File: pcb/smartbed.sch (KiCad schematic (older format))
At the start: 20 parts, among them U1 ATSAMD21J18A

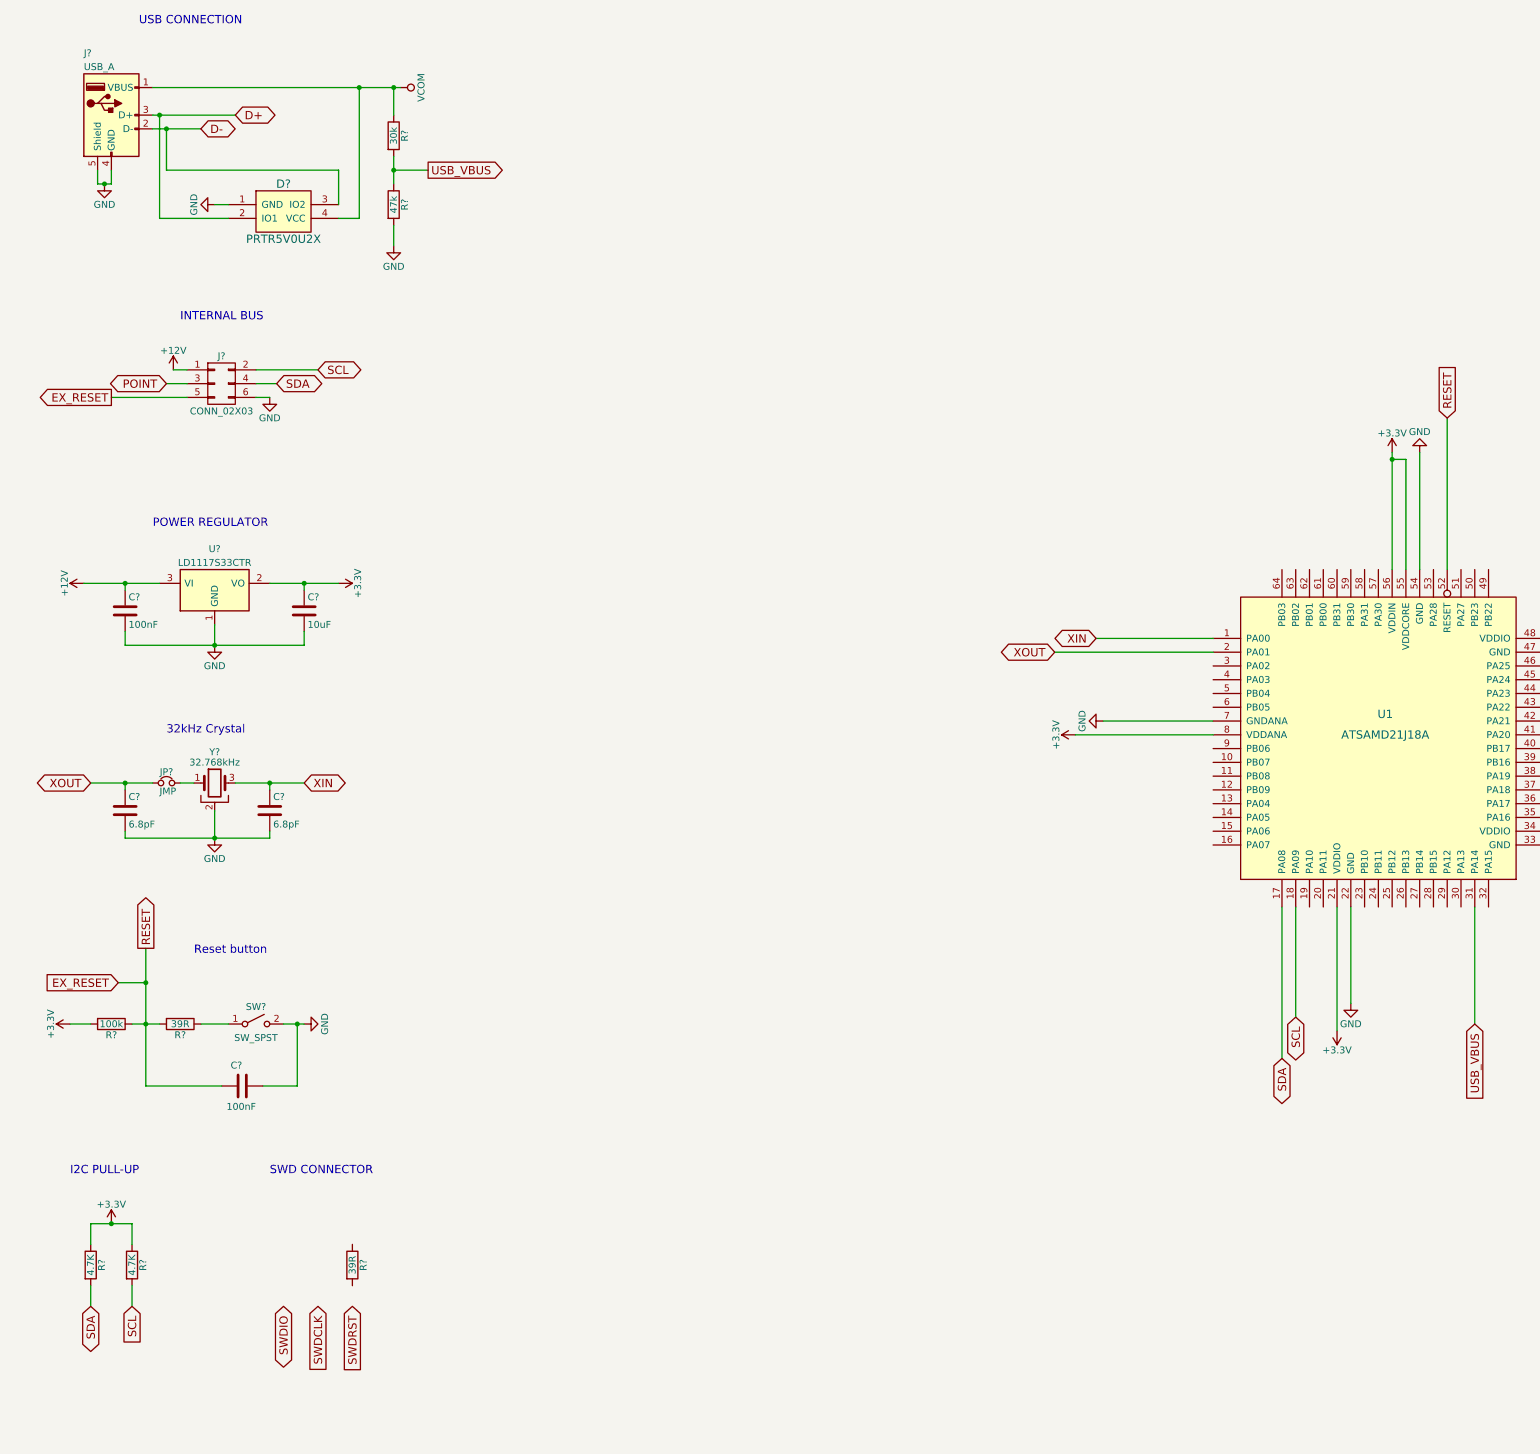
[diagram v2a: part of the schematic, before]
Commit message: Added debug connector and capacitors
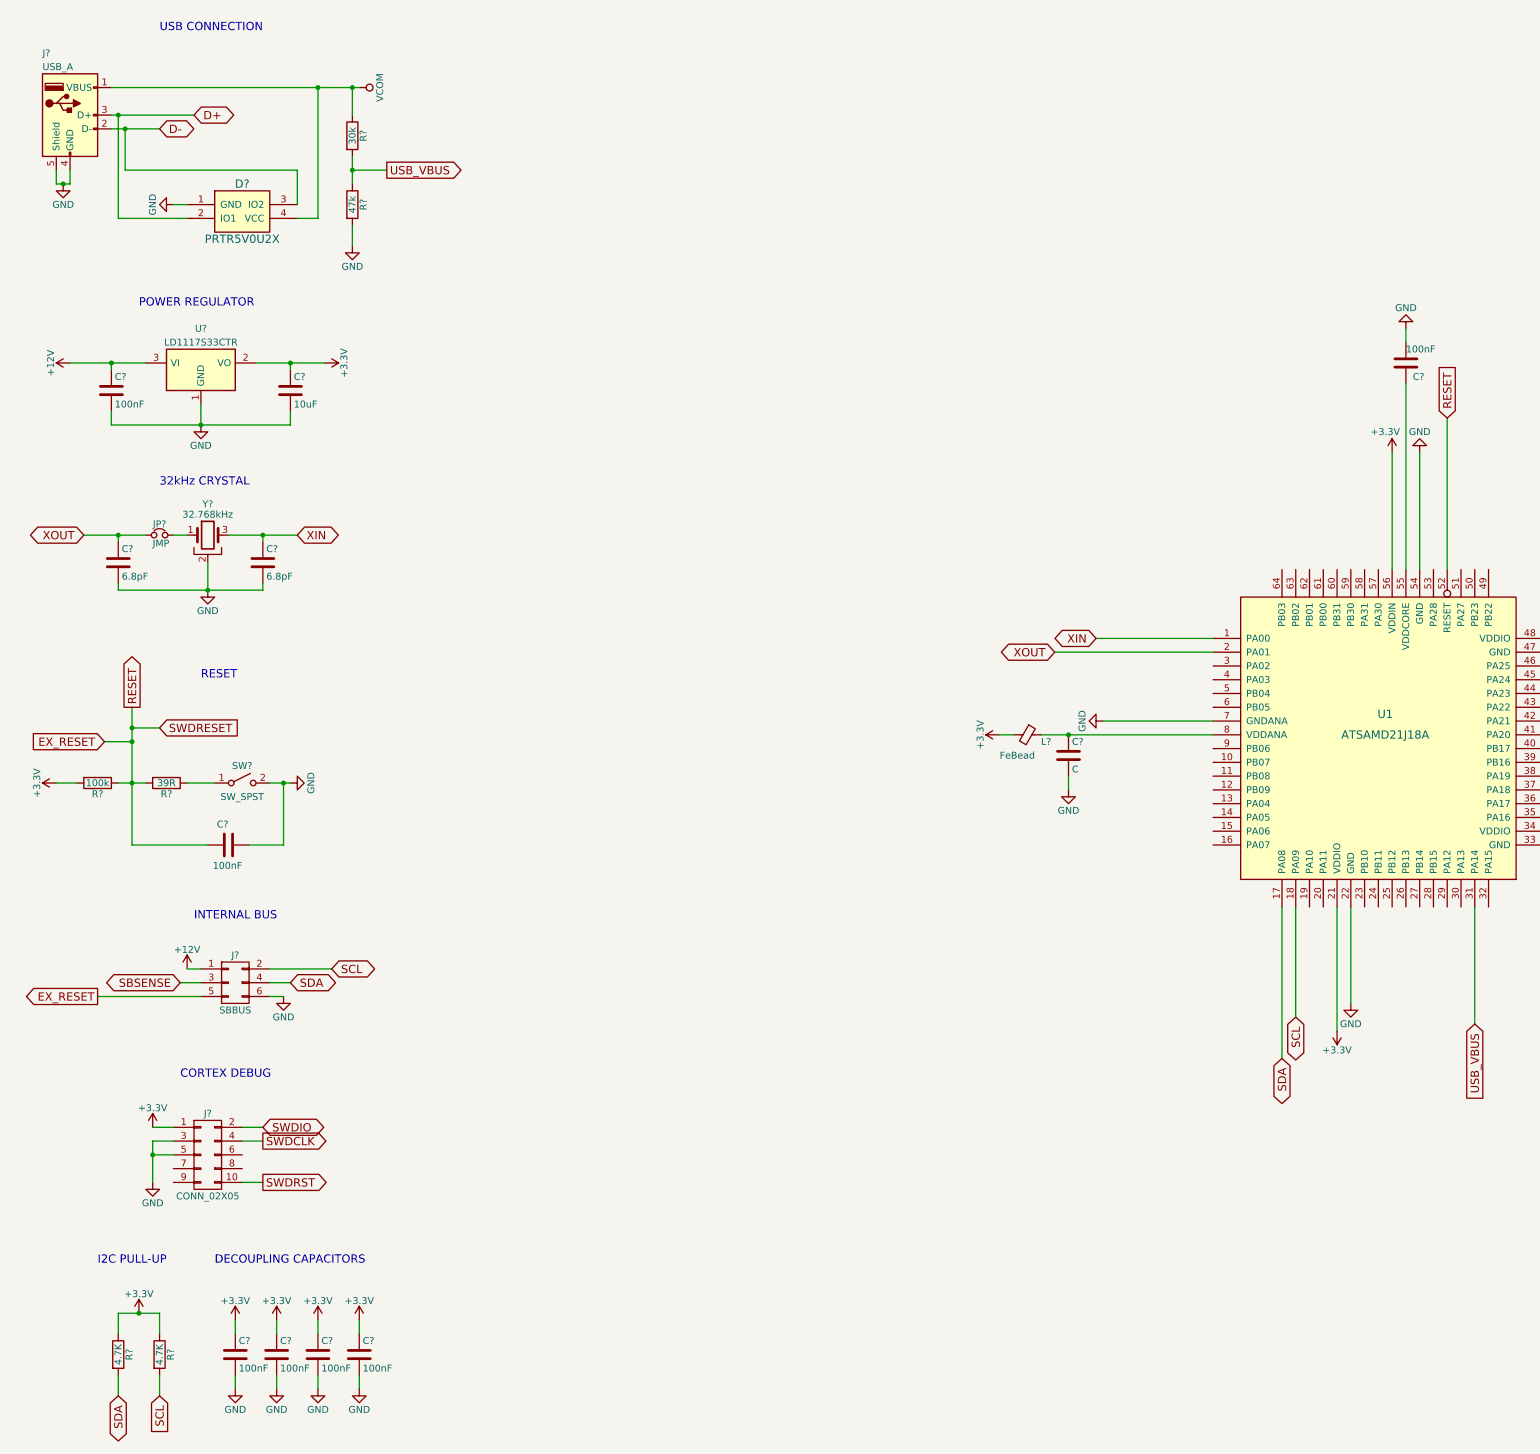
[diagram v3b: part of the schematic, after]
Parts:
- removed R?: 39R, symbol R
- added C? (x5): 100nF, symbol C
- added C?: C, symbol C
- added J?: CONN_02X05, symbol CONN_02X05
- added L?: FeBead, symbol Ferrite_Bead_Small
- J?: value CONN_02X03 -> SBBUS
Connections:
- net +3V3: now also C?.1, C?.1, C?.1, C?.1, J?.1 (P1), L?.2; no longer U1.55 (VDDCORE), U1.8 (VDDANA)
- net GND: now also C?.1, C?.2, C?.2, C?.2, C?.2, C?.2, J?.3 (P3), J?.5 (P5)
- net SWDCLK: now also J?.4 (P4)
- net SWDIO: now also J?.2 (P2)
- net SWDRST: now also J?.10 (P10)
- net POINT renamed SBSENSE
- new net: C?.2, U1.55 (VDDCORE)
- new net: C?.1, L?.1, U1.8 (VDDANA)
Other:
- note added: "32kHz CRYSTAL"
- note added: "CORTEX DEBUG"
- note added: "DECOUPLING CAPACITORS"
- note added: "RESET"
- note removed: "32kHz Crystal"
- note removed: "Reset button"
- note removed: "SWD CONNECTOR"
- moved on the sheet: C?, D?, J?, JP?, R?, SW?, U?, Y?

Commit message: Added FSR connectors
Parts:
- removed R?: 30k, symbol R
- removed R?: 47k, symbol R
- added C?: 100nF, symbol C
- added D? (x2): LED G, symbol LED_Small
- added J? (x2): CONN_02X08, symbol CONN_02X08
- added R? (x2): 330R, symbol R
- added R? (x16): 10K, symbol R
- C?: value C -> 100nF
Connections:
- net SBSENSE is gone; now on net SENSE_IN: J?.3 (P3)
- net VCOM is gone; now on net +5V: D?.4 (VCC), J?.1 (VBUS)
- net +3V3: now also R?.1, R?.1, R?.2, R?.2, R?.2, R?.2, R?.2, R?.2, R?.2, R?.2, R?.2, R?.2, R?.2, R?.2, R?.2, R?.2, R?.2, R?.2
- net EX_RESET: no longer J?.5 (P5)
- net GND: now also C?.1, D?.1 (K), J?.10 (P10), J?.10 (P10), J?.12 (P12), J?.12 (P12), J?.14 (P14), J?.14 (P14), J?.16 (P16), J?.16 (P16), J?.2 (P2), J?.2 (P2), J?.4 (P4), J?.4 (P4), J?.6 (P6), J?.6 (P6), J?.8 (P8), J?.8 (P8)
- net SWDCLK: now also U1.57 (PA30)
- net SWDIO: now also U1.58 (PA31)
- net FSR15: now reaches U1.10 (PB07)
- net FSR15: now also J?.15 (P15), R?.1
- net FSR2: now reaches U1.11 (PB08)
- net FSR2: now also J?.5 (P5), R?.1
- net FSR3: now reaches U1.12 (PB09)
- net FSR3: now also J?.7 (P7), R?.1
- net FSR4: now reaches U1.13 (PA04)
- net FSR4: now also J?.9 (P9), R?.1
- net FSR5: now reaches U1.14 (PA05)
- net FSR5: now also J?.11 (P11), R?.1
- net FSR6: now reaches U1.15 (PA06)
- net FSR6: now also J?.13 (P13), R?.1
- net FSR7: now reaches U1.16 (PA07)
- net FSR7: now also J?.15 (P15), R?.1
- net FSR0: now reaches U1.3 (PA02)
- net FSR0: now also J?.1 (P1), R?.1
- net FSR1: now reaches U1.4 (PA03)
- net FSR1: now also J?.3 (P3), R?.1
- net FSR12: now reaches U1.5 (PB04)
- net FSR12: now also J?.9 (P9), R?.1
- net SENSE_OUT: now reaches U1.51 (PA27)
- net SENSE_OUT: now also J?.5 (P5)
- net SENSE_IN: now reaches U1.53 (PA28)
- net DBGLED: now reaches U1.59 (PB30)
- net DBGLED: now also D?.1 (K)
- net FSR13: now reaches U1.6 (PB05)
- net FSR13: now also J?.11 (P11), R?.1
- net FSR8: now reaches U1.61 (PB00)
- net FSR8: now also J?.1 (P1), R?.1
- net FSR9: now reaches U1.62 (PB01)
- net FSR9: now also J?.3 (P3), R?.1
- net FSR10: now reaches U1.63 (PB02)
- net FSR10: now also J?.5 (P5), R?.1
- net FSR11: now reaches U1.64 (PB03)
- net FSR11: now also J?.7 (P7), R?.1
- net FSR14: now reaches U1.9 (PB06)
- net FSR14: now also J?.13 (P13), R?.1
- net +12V renamed +5V
- net +5V: now also C?.2
- new net: D?.2 (A), R?.2 (x2)
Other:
- note added: "POWER / DBG LEDS"
- note added: "PRESSURE SENSOR CONNECTORS"
- moved on the sheet: C?, D?, J?, L?, R?, U1, U?

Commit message: Assigned footprints, started PCB
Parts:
- removed U1: ATSAMD21J18A, Housings_QFP:TQFP-64_10x10mm_Pitch0.5mm, symbol ATSAMD21J18A
- added J4, J5: GPIOCON, Pin_Headers:Pin_Header_Straight_2x08_Pitch2.54mm, symbol CONN_02X08
- added J8: SBBUS_2, Pin_Headers:Pin_Header_Straight_2x03_Pitch2.54mm, symbol CONN_02X03
- added R5: 30k, Resistors_SMD:R_0805_HandSoldering, symbol R
- added R6: 47k, Resistors_SMD:R_0805_HandSoldering, symbol R
- added U2: ATSAMD21J18A, Housings_QFP:TQFP-64_10x10mm_Pitch0.5mm, symbol ATSAMD21J18A
- C1, C10, C11, C12, C2, C3, C4, C5, C6, C7, C8, C9: renamed from C?; footprint (none) -> Capacitors_SMD:C_0805_HandSoldering
- D1: renamed from D?; footprint (none) -> TO_SOT_Packages_SMD:SOT-143_Handsoldering
- D2, D3: renamed from D?; footprint (none) -> LEDs:LED_0805
- J1: renamed from J?; value USB_A -> USB_MICRO_A; footprint (none) -> Connectors:USB_Micro-B
- J2: renamed from J?; value SBBUS -> SBBUS_1; footprint (none) -> Pin_Headers:Pin_Header_Straight_2x03_Pitch2.54mm
- J3: renamed from J?; value CONN_02X05 -> DBGCON; footprint (none) -> Pin_Headers:Pin_Header_Straight_2x05_Pitch2.54mm
- J6: renamed from J?; value CONN_02X08 -> FSRCON1; footprint (none) -> Pin_Headers:Pin_Header_Angled_2x08_Pitch2.54mm
- J7: renamed from J?; value CONN_02X08 -> FSRCON2; footprint (none) -> Pin_Headers:Pin_Header_Angled_2x08_Pitch2.54mm
- JP1: renamed from JP?; footprint (none) -> Pin_Headers:Pin_Header_Straight_1x02_Pitch2.54mm
- L1: renamed from L?; footprint (none) -> Inductors_SMD:L_0603_HandSoldering
- R1, R10, R11, R12, R13, R14, R15, R16, R17, R18, R19, R2, R20, R21, R22, R23, R24, R25, R3, R4, R7, R8: renamed from R?; footprint (none) -> Resistors_SMD:R_0805_HandSoldering
- SW1: renamed from SW?; footprint (none) -> Buttons_Switches_SMD:SW_SPST_B3SL-1002P
- Y1: renamed from Y?; footprint (none) -> Crystals:Crystal_Round_d3.0mm_Vertical
- gave numbers to parts that had none: 1
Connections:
- net SWDRST is gone; now on net RESET: J3.10 (P10)
- net +3V3: now also J4.16 (P16), J5.16 (P16), U2.21 (VDDIO), U2.34 (VDDIO), U2.48 (VDDIO), U2.56 (VDDIN)
- net +5V: now also J8.1 (P1), R5.1
- net D+: now also U2.46 (PA25)
- net D-: now also U2.45 (PA24)
- net DBGLED: now also U2.59 (PB30)
- net FSR0: now also U2.3 (PA02)
- net FSR1: now also U2.4 (PA03)
- net FSR10: now also U2.63 (PB02)
- net FSR11: now also U2.64 (PB03)
- net FSR12: now also U2.5 (PB04)
- net FSR13: now also U2.6 (PB05)
- net FSR14: now also U2.9 (PB06)
- net FSR15: now also U2.10 (PB07)
- net FSR2: now also U2.11 (PB08)
- net FSR3: now also U2.12 (PB09)
- net FSR4: now also U2.13 (PA04)
- net FSR5: now also U2.14 (PA05)
- net FSR6: now also U2.15 (PA06)
- net FSR7: now also U2.16 (PA07)
- net FSR8: now also U2.61 (PB00)
- net FSR9: now also U2.62 (PB01)
- net GND: now also J4.1 (P1), J5.1 (P1), J8.6 (P6), R6.2, U2.22 (GND), U2.33 (GND), U2.47 (GND), U2.54 (GND), U2.7 (GNDANA)
- net SCL: now also J5.12 (P12), J8.2 (P2), U2.18 (PA09)
- net SDA: now also J5.14 (P14), J8.4 (P4), U2.17 (PA08)
- net SENSE_IN: now also J4.12 (P12), J8.5 (P5), U2.53 (PA28)
- net SENSE_OUT: now also J4.14 (P14), J8.3 (P3), U2.51 (PA27)
- net SWDCLK: now also U2.57 (PA30)
- net SWDIO: now also U2.58 (PA31)
- net XIN: now also U2.1 (PA00)
- net XOUT: now also U2.2 (PA01)
- net at C12.2: now also U2.55 (VDDCORE)
- net at C11.1, L1.1: now also U2.8 (VDDANA)
- net EX_RESET renamed RESET
- net RESET: now also U2.52 (RESET)
- new net PA10: J5.10 (P10), U2.19 (PA10)
- new net PA11: J5.8 (P8), U2.20 (PA11)
- new net PA12: J5.9 (P9), U2.29 (PA12)
- new net PA13: J5.7 (P7), U2.30 (PA13)
- new net PA15: J5.5 (P5), U2.32 (PA15)
- new net PA16: J5.3 (P3), U2.35 (PA16)
- new net PA17: J4.10 (P10), U2.36 (PA17)
- new net PA18: J4.8 (P8), U2.37 (PA18)
- new net PA19: J4.6 (P6), U2.38 (PA19)
- new net PA20: J4.13 (P13), U2.41 (PA20)
- new net PA21: J4.15 (P15), U2.42 (PA21)
- new net PA22: J4.11 (P11), U2.43 (PA22)
- new net PA23: J4.9 (P9), U2.44 (PA23)
- new net PB10: J5.6 (P6), U2.23 (PB10)
- new net PB11: J5.4 (P4), U2.24 (PB11)
- new net PB12: J5.2 (P2), U2.25 (PB12)
- new net PB13: J5.15 (P15), U2.26 (PB13)
- new net PB14: J5.13 (P13), U2.27 (PB14)
- new net PB15: J5.11 (P11), U2.28 (PB15)
- new net PB16: J4.4 (P4), U2.39 (PB16)
- new net PB17: J4.2 (P2), U2.40 (PB17)
- new net PB22: J4.7 (P7), U2.49 (PB22)
- new net PB23: J4.5 (P5), U2.50 (PB23)
- new net PB31: J4.3 (P3), U2.60 (PB31)
- new net VBUS: R5.2, R6.1, U2.31 (PA14)
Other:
- note added: "GPIO BREAKOUT CONNECTORS"
- moved on the sheet: C11, C12, L1
